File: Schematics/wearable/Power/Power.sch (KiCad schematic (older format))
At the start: 6 parts, among them IC1 BQ25120AYFPR, J1 USB_B_Micro, J2 JST-XH BAT, Q1 CSD83325LT, U1 BQ29702DSET

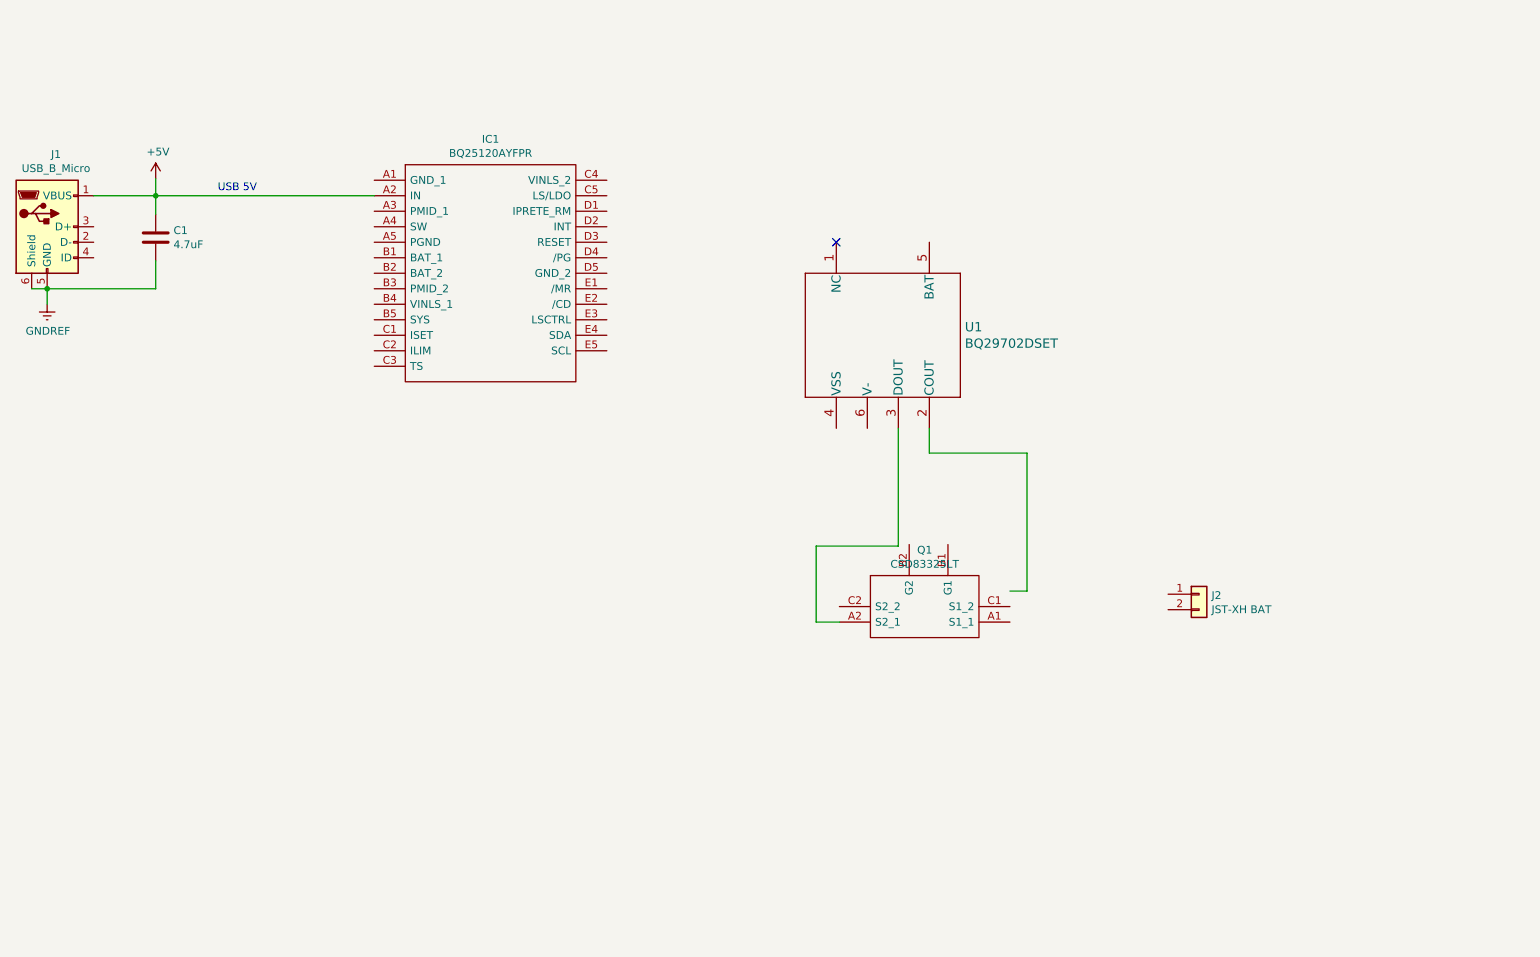
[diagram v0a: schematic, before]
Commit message: Created and finished schematic for power and BMS
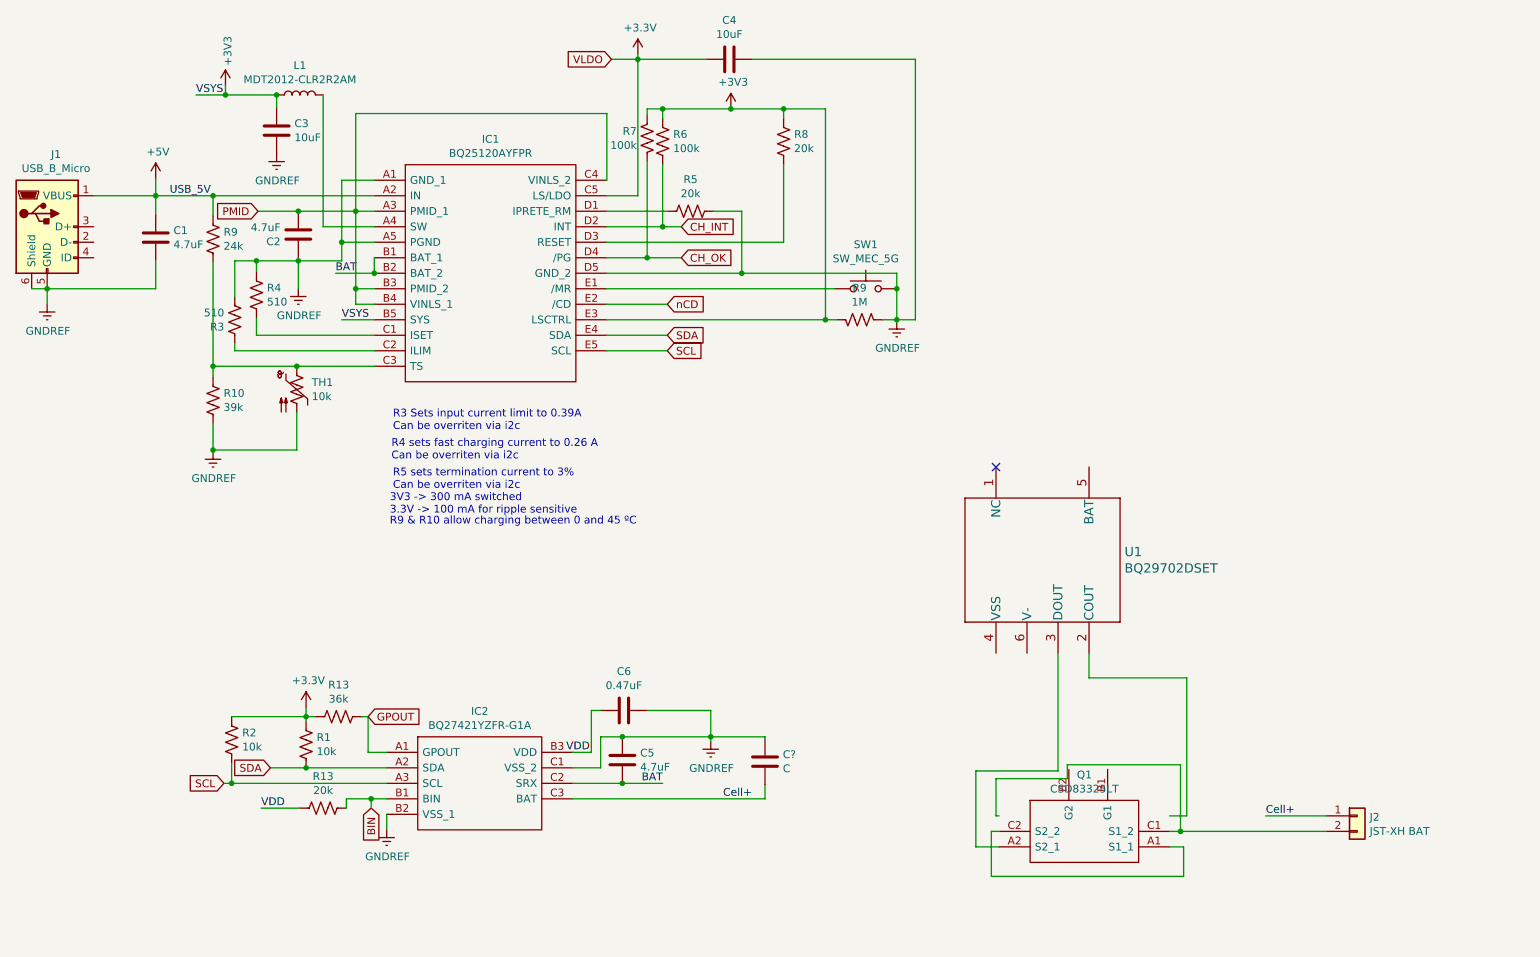
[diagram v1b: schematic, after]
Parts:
- added C2, C5: 4.7uF, symbol Device:C
- added C3, C4: 10uF, symbol Device:C
- added C6: 0.47uF, symbol Device:C
- added C?: C, symbol Device:C
- added IC2: BQ27421YZFR-G1A, BGA9C50P3X3_162X158X62, symbol SamacSys_Parts:BQ27421YZFR-G1A
- added L1: MDT2012-CLR2R2AM, symbol Device:L
- added R1, R2: 10k, symbol Device:R_US
- added R10: 39k, symbol Device:R_US
- added R13: 36k, symbol Device:R_US
- added R13, R5, R8: 20k, symbol Device:R_US
- added R3, R4: 510, symbol Device:R_US
- added R6, R7: 100k, symbol Device:R_US
- added R9: 1M, symbol Device:R_US
- added R9: 24k, symbol Device:R_US
- added SW1: SW_MEC_5G, symbol Switch:SW_MEC_5G
- added TH1: 10k, symbol Device:Thermistor_PTC_US
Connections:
- net labels added: +3.3V, +3V3, BAT, BIN, CH_INT, CH_OK, Cell+, GPOUT, PMID, SCL, SDA, USB_5V, VDD, VLDO, VSYS, nCD
- wire segments 16 -> 147
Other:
- note added: "3V3 -> 300 mA switched\n3.3V -> 100 mA for ripple sensitive\n\n"
- note added: "R3 Sets input current limit to 0.39A\nCan be overriten via i2c"
- note added: "R4 sets fast charging current to 0.26 A\nCan be overriten via i2c\n"
- note added: "R5 sets termination current to 3%\nCan be overriten via i2c"
- note added: "R9 & R10 allow charging between 0 and 45 ºC\n"
- note removed: "USB 5V\n"
- moved on the sheet: J2, Q1, U1

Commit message: Readability
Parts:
- removed C?: C, symbol Device:C
- added C?: C_Small, symbol Device:C_Small
- added R?: 2.2k, symbol Device:R_Small
- added R? (x2): 5.1M, symbol Device:R_Small
- added R?: 0.56, symbol Device:R_Small
- added R?: DNI, symbol Device:R_Small
- added R?: 330, symbol Device:R_Small
- C5, C6: symbol Device:C -> Device:C_Small
- U1: symbol eec:BQ29702DSET -> SamacSys_Parts:BQ29700DSET
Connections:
- net Cell+: now also R?.2
- net GNDREF: now also R?.1, R?.1, R?.2, R?.2
- net at Q1.A1 (S1_1): now also J2.2 (Pin_2), Q1.C1 (S1_2), U1.4 (VSS), C?.2, R?.1, R?.2; no longer Q1.C2 (S2_2)
- net at Q1.A2 (S2_1): now also Q1.C2 (S2_2), R?.2; no longer U1.3 (DOUT)
- net at Q1.B1 (G1): now also U1.3 (DOUT), R?.2
- net at Q1.B2 (G2): now also U1.2 (COUT), R?.1
- net at U1.5 (BAT): now also C?.1, R?.1
- net at U1.6 (V-): now also R?.1
- no-connect marks 1 -> 0
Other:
- moved on the sheet: J2, Q1
